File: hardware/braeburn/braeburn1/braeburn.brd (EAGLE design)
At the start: 100 x 80 mm, 32 parts, among them IC1 MAX481CSA, IC2 MEGA8-AI, IC3 MAX4105EUK, IC4 MAX4105EUK, IC5 MAX4105EUK, X1 5566-20

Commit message: braeburn version
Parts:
- added D1: 3V3, diode:DO41Z10
- added JP3: AVR-ISP-6VERT, avr-7:AVR-ISP-6
- added JP4: (no value), pinhead:1X02
- added R3: (no value), rcl:R0603
- added SJ1, SJ2: (no value), jumper:SJW
- added U$2: HGG_LOGO, hgg:HGG_LOGO
- added X2: (no value), con-molex:KK-156-4
- C13: value (none) -> 100nF
- Q1: value (none) -> 16-20MHz
- moved IC5 92.0 mm to (70.6, 42.4), turned to 140.4 degrees
- moved IC4 84.4 mm to (65.3, 44.2), turned to 147.2 degrees
- moved IC3 75.6 mm to (59.3, 45.0), turned to 142.6 degrees
- moved C10 32.5 mm to (65.1, 20.6), turned to 316.9 degrees
- moved C7 22.4 mm to (4.50, 35.3), turned to 180 degrees
- moved R1 21.2 mm to (92.3, 41.5), turned to 270 degrees
- moved JP1 20.1 mm to (89.9, 55.6), flipped to the bottom
- moved JP2 20.0 mm to (89.9, 50.5), flipped to the bottom
- moved IC2 19.6 mm to (69.6, 25.3), turned to 47.8 degrees
- moved C11 17.8 mm to (63.4, 13.8), turned to 139 degrees
- moved Q1 16.6 mm to (66.3, 14.3), flipped to the bottom, turned to 43.2 degrees
- moved C5 15.9 mm to (25.7, 37.1), turned to 180 degrees
- moved S1 14.5 mm to (87.6, 42.0), flipped to the bottom, turned to 270 degrees
- moved C12 13.0 mm to (65.7, 11.4), turned to 318.3 degrees
- moved C13 12.1 mm to (74.2, 31.7), turned to 135 degrees
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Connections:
- removed net N$16: IC3.2, IC4.2
- removed net N$7: IC2.17
- removed net VCC: C10.1, IC1.8, R1.2
- new net MISO: IC2.16, JP3.1
- new net MOSI: IC2.15, JP3.4
- new net N$15: D1.A, SJ1.1, SJ2.1
- new net SCK: IC2.17, JP3.3
- net AVCC: no longer IC2.20
- net GND: now also D1.C, JP3.6, JP4.1, X2.2, X2.3
- net IN_+12V: now also X2.4
- net IN_+3V3: now also X1.1
- net IN_+5V: now also R3.2, SJ2.2, X2.1
- net IN_-5V: now also IC3.2, IC4.2
- net MEASURE_12V: now also IC2.23; no longer IC2.25
- net MEASURE_3V3: now also IC2.25; no longer IC2.23
- net N$8: now also JP4.2, R3.1; no longer IC2.16
- net OUT_+3V3: now also C10.1, IC1.8, JP3.2, R1.2, SJ1.2
- net OUT_+5V: now also IC2.20
- net R/W: now also IC2.26
- net RST: now also JP3.5
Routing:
- net GND: track 0.00 -> 422.3 mm, vias 0 -> 20
- net IN_+5V: track 0.00 -> 156.2 mm, vias 0 -> 2
- net OUT_+3V3: track 0.00 -> 139.1 mm, vias 0 -> 6
- net IN_+12V: track 0.00 -> 98.5 mm, vias 0 -> 3
- net OUT_+5V: track 0.00 -> 98.4 mm, vias 0 -> 3
- net CARD-PRESENT: track 0.00 -> 87.6 mm, vias 0 -> 4
- net OUT_+12V: track 0.00 -> 86.7 mm, vias 0 -> 2
- net IN_-5V: track 0.00 -> 80.6 mm, vias 0 -> 4
- net 12V_2: track 0.00 -> 78.0 mm, vias 0 -> 2
- net PSON: track 0.00 -> 63.1 mm, vias 0 -> 2
- net 5V_2: track 0.00 -> 62.4 mm, vias 0 -> 2
- net RST: track 0.00 -> 60.1 mm, vias 0 -> 4
- net IN_+3V3: track 0.00 -> 38.9 mm
- net IRQ: track 0.00 -> 37.3 mm, vias 0 -> 2
- net INTACK: track 0.00 -> 35.1 mm
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- added copper zone on layer 1, net GND
- added copper zone on layer 16, net GND
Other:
- board size 100 x 80 mm -> 95.5 x 62 mm
- board text added: "braeburn v1.0"
- board text added: "cc-by-nc-sa"

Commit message: new braeburn version for using a PC ps
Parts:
- removed U$2: HGG_LOGO, hgg:HGG_LOGO
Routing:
- net GND: track 422.3 -> 363.5 mm, vias 20 -> 29
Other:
- board text added: "braeburn v2"
- board text added: "http://hgg.aero"
- board text removed: "braeburn v1.0"

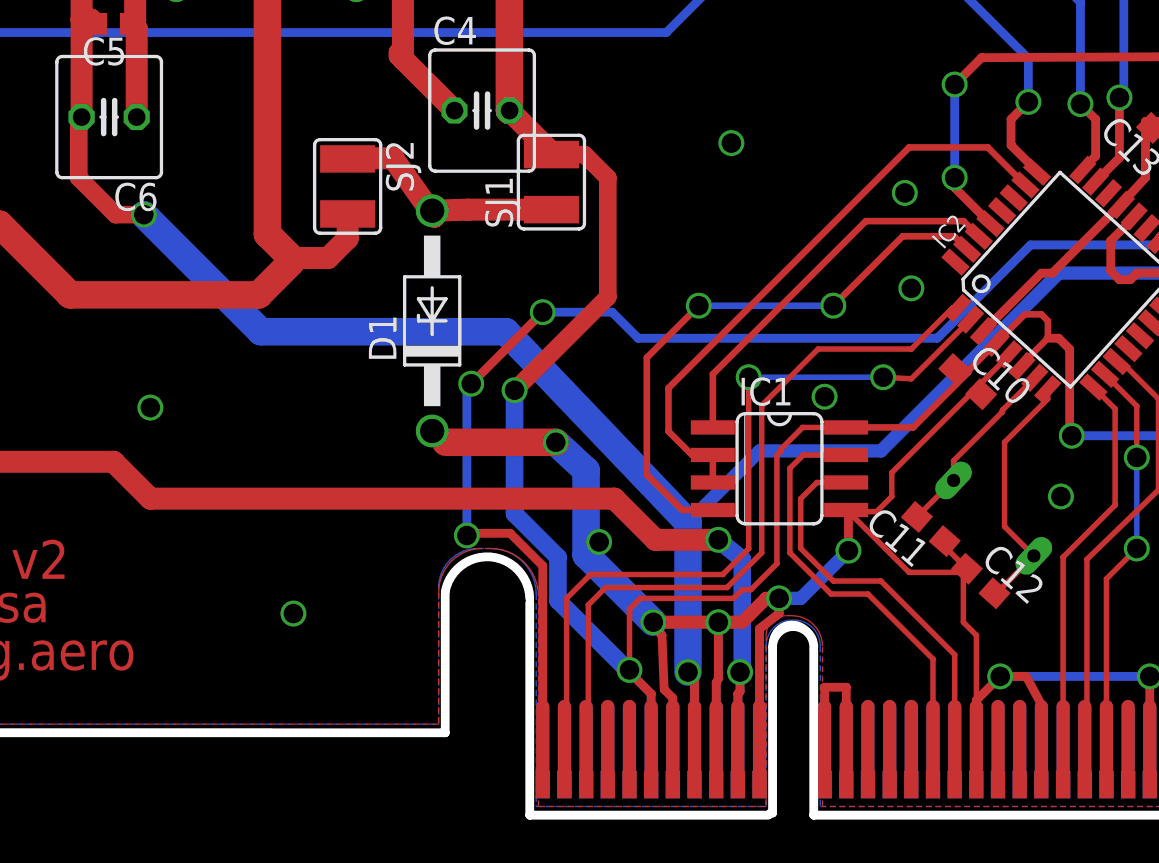
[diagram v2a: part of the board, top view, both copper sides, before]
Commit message: changes to solve problems with the first design
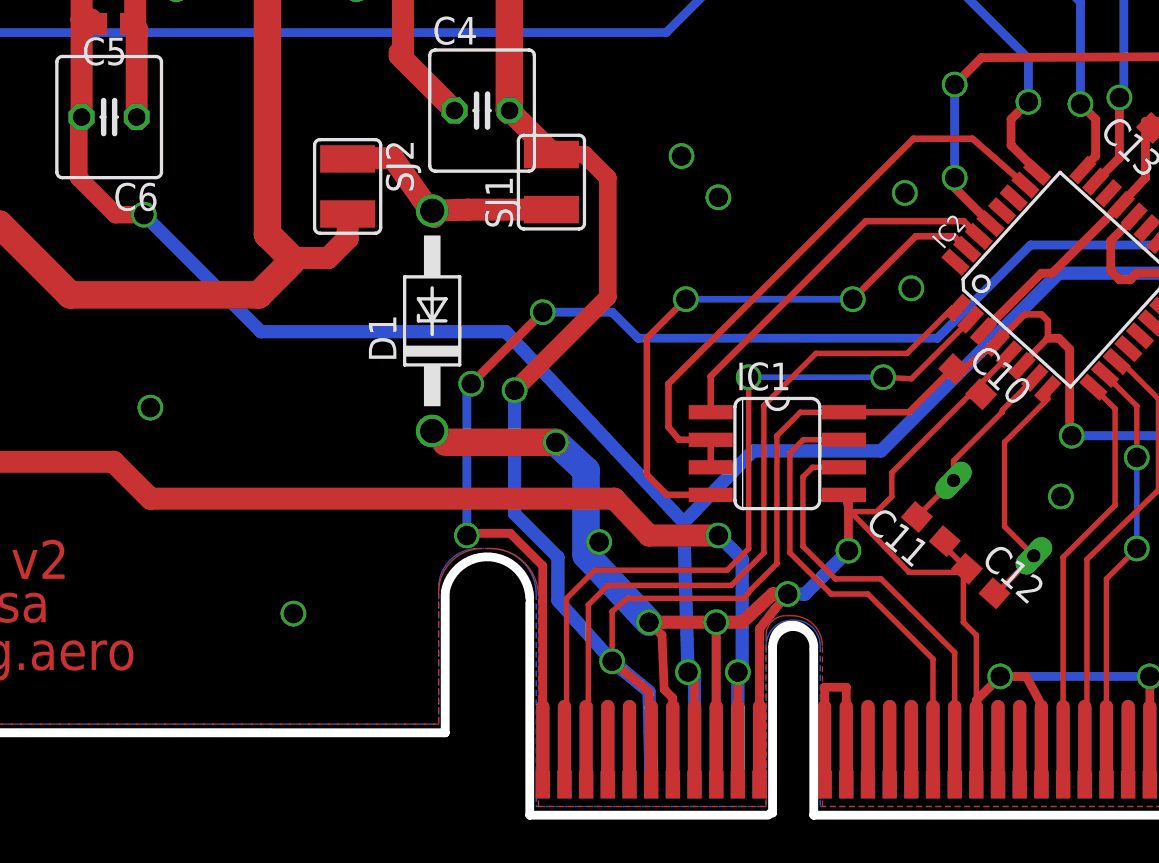
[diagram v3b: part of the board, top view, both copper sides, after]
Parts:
- moved IC1 0.71 mm to (56.3, 17.3)
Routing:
- net GND: track 363.5 -> 366.1 mm
- net OUT_+3V3: track 139.1 -> 140.2 mm
- net RX: track 17.9 -> 17.3 mm
- net BUS0-: track 21.2 -> 21.8 mm
- net BUS0+: track 19.8 -> 20.4 mm
